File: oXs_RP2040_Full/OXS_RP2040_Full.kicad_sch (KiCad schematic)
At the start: 63 parts, among them J1 TLM/CRSF, J10 SPARE, J11 RMP, J2 V1/V2, J3 V3/V4, J4 GPS, J5 SELECT_POWER, J6 SBUS, J7 LIPO 8S, J8 MPU6050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

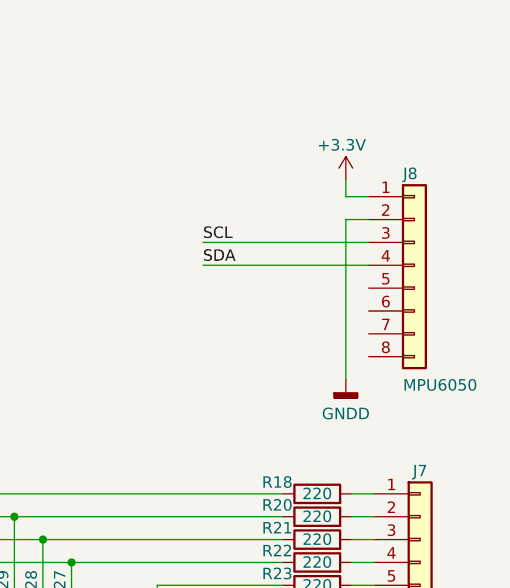
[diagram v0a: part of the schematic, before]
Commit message: replace mpu6050 connection
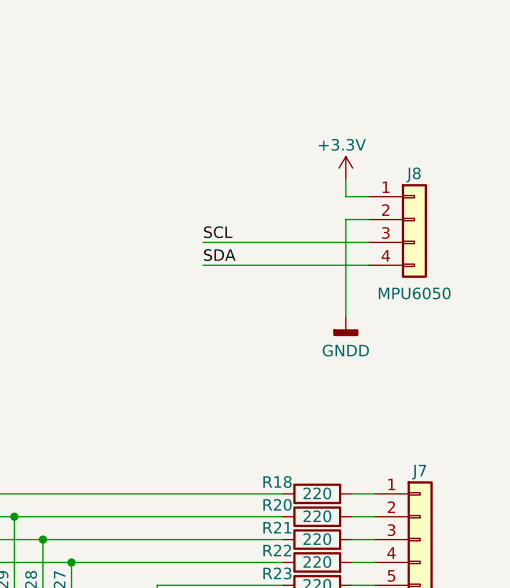
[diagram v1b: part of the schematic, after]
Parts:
- removed J8: MPU6050, Connector_PinHeader_2.54mm:PinHeader_1x08_P2.54mm_Vertical, symbol Connector_Generic:Conn_01x08
- added J8: MPU6050, Connector_PinHeader_2.54mm:PinHeader_1x04_P2.54mm_Vertical, symbol Connector_Generic:Conn_01x04
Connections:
- net +3.3V: now also J8.1 (Pin_1)
- net GNDD: now also J8.2 (Pin_2)
- net SCL: now also J8.3 (Pin_3)
- net SDA: now also J8.4 (Pin_4)
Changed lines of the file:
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@@
   (title_block
     (title "openXsensor RP2040 Full")
-    (date "2023-03-28")
+    (date "2023-04-02")
     (rev "0.1")
     (comment 1 "SW: mstrens    PCB: pierrotm777")
@@
     (stroke (width 0) (type default))
   )
-  (wire (pts (xy 259.715 60.96) (xy 259.715 43.18))
+  (wire (pts (xy 259.715 53.975) (xy 259.715 43.18))
     (stroke (width 0) (type default))
   )
@@
     )
   )
-  (symbol (lib_id "Connector_Generic:Conn_01x08") (at 267.335 48.26 0) (unit 1)
-    (in_bom yes) (on_board yes) (dnp no)
-    (property "Reference" "J8" (at 266.065 38.1 0)
-      (effects (font (size 1.27 1.27)) (justify left))
-    )
-    (property "Value" "MPU6050" (at 266.065 61.595 0)
-      (effects (font (size 1.27 1.27)) (justify left))
-    )
-    (property "Footprint" "Connector_PinHeader_2.54mm:PinHeader_1x08_P2.54mm_Vertical" (at 267.335 48.26 0)
-      (effects (font (size 1.27 1.27)) hide)
-    )
-    (property "Datasheet" "~" (at 267.335 48.26 0)
-      (effects (font (size 1.27 1.27)) hide)
-    )
-    (pin "1")
-    (pin "2")
-    (pin "3")
-    (pin "4")
-    (pin "5")
-    (pin "6")
-    (pin "7")
-    (pin "8")
-    (instances
-      (project "OXS_RP2040_Full"
-        (path "/68d7a088-7c28-4087-951c-c5d6e26d9b30"
-          (reference "J8") (unit 1)
-        )
-      )
-    )
-  )
   (symbol (lib_id "power:GNDD") (at 57.15 147.32 0) (unit 1)
     (in_bom yes) (on_board yes) (dnp no)
@@
     )
   )
+  (symbol (lib_id "Connector_Generic:Conn_01x04") (at 267.335 43.18 0) (unit 1)
+    (in_bom yes) (on_board yes) (dnp no)
+    (property "Reference" "J8" (at 267.335 38.1 0)
+      (effects (font (size 1.27 1.27)))
+    )
+    (property "Value" "MPU6050" (at 267.335 51.435 0)
+      (effects (font (size 1.27 1.27)))
+    )
+    (property "Footprint" "Connector_PinHeader_2.54mm:PinHeader_1x04_P2.54mm_Vertical" (at 267.335 43.18 0)
+      (effects (font (size 1.27 1.27)) hide)
+    )
+    (property "Datasheet" "~" (at 267.335 43.18 0)
+      (effects (font (size 1.27 1.27)) hide)
+    )
+    (pin "1")
+    (pin "2")
+    (pin "3")
+    (pin "4")
+    (instances
+      (project "OXS_RP2040_Full"
+        (path "/68d7a088-7c28-4087-951c-c5d6e26d9b30"
+          (reference "J8") (unit 1)
+        )
+      )
+    )
+  )
   (symbol (lib_id "power:GNDD") (at 195.58 133.985 0) (unit 1)
     (in_bom yes) (on_board yes) (dnp no)
@@
     )
   )
-  (symbol (lib_id "power:GNDD") (at 259.715 60.96 0) (unit 1)
+  (symbol (lib_id "power:GNDD") (at 259.715 53.975 0) (unit 1)
     (in_bom yes) (on_board yes) (dnp no)
-    (property "Reference" "#PWR043" (at 259.715 67.31 0)
+    (property "Reference" "#PWR043" (at 259.715 60.325 0)
       (effects (font (size 1.27 1.27)) hide)
     )
-    (property "Value" "GNDD" (at 259.715 64.77 0)
+    (property "Value" "GNDD" (at 259.715 57.785 0)
       (effects (font (size 1.27 1.27)))
     )
-    (property "Footprint" "" (at 259.715 60.96 0)
+    (property "Footprint" "" (at 259.715 53.975 0)
       (effects (font (size 1.27 1.27)) hide)
     )
-    (property "Datasheet" "" (at 259.715 60.96 0)
+    (property "Datasheet" "" (at 259.715 53.975 0)
       (effects (font (size 1.27 1.27)) hide)
     )

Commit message: update / build gerber
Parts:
- J7: value LIPO 8S -> 8 INPUT ALARMS
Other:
- note added: "ADD=0x68"
- note added: "ADD=0x76"
- moved on the sheet: C6, C9, J10, J11, J7, J8, R10, R11, R12, R14, R15, R16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
